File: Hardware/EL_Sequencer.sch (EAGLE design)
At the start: 109 parts, among them U1 LM317, U10 Z0103MN, U11 Z0103MN, U12 Z0103MN, U13 MOC3063S, U14 MOC3063S, U15 MOC3063S, U16 MOC3063S, U17 Z0103MN, U18 Z0103MN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

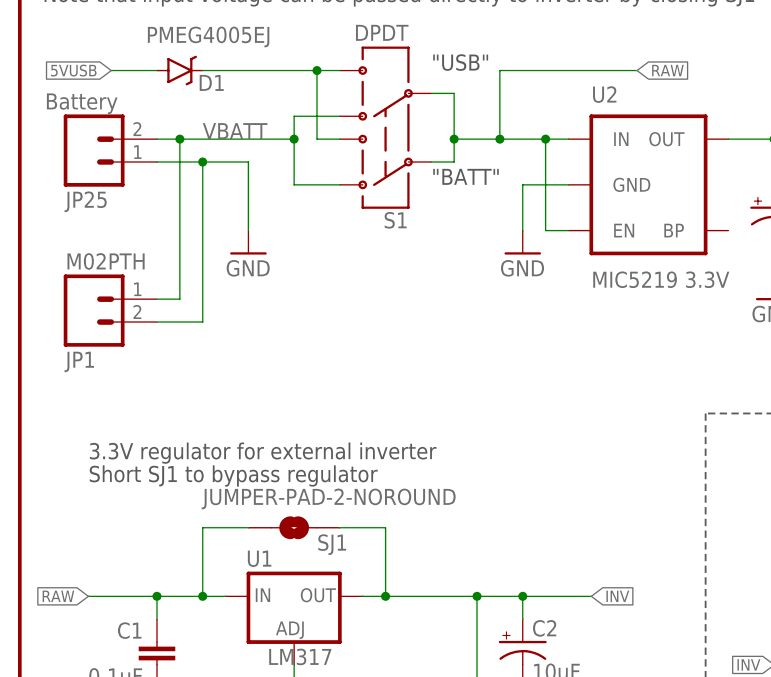
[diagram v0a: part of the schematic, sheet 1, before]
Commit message: Bumping up drill hits in side smd switch
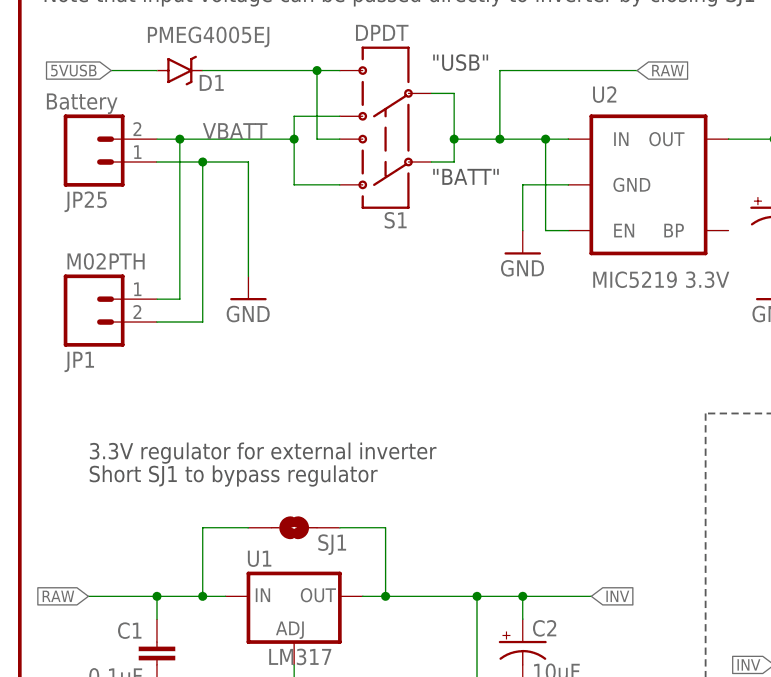
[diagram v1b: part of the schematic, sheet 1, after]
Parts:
- S3: device SparkFun-Electromechanical:SWITCH_SPDT -> Testing:SWITCH_SPDT
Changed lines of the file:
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@@
 <layer number="251" name="SMDround" color="12" fill="11" visible="no" active="no"/>
 <layer number="254" name="cooling" color="7" fill="1" visible="yes" active="yes"/>
+<layer number="255" name="routoute" color="7" fill="1" visible="yes" active="yes"/>
 </layers>
 <schematic xreflabel="%F%N" xrefpart="/%S">
@@
 <part name="FID2" library="SparkFun-Aesthetics" deviceset="FIDUCIAL" device="1X2"/>
 <part name="D1" library="SparkFun-DiscreteSemi" deviceset="DIODE-SCHOTTKY" device="-PMEG4005EJ" value="PMEG4005EJ"/>
-<part name="S3" library="SparkFun-Electromechanical" deviceset="SWITCH_SPDT" device=""/>
+<part name="S3" library="Testing" deviceset="SWITCH_SPDT" device=""/>
 </parts>
 <sheets>
@@
 <attribute name="VALUE" x="2.794" y="162.56" size="1.778" layer="96" rot="MR180"/>
 </instance>
-<instance part="GND1" gate="1" x="25.4" y="144.78"/>
+<instance part="GND1" gate="1" x="25.4" y="139.7"/>
 <instance part="U2" gate="G$1" x="71.12" y="152.4"/>
 <instance part="GND3" gate="1" x="55.88" y="144.78"/>
@@
 <instance part="SJ1" gate="G$1" x="30.48" y="114.3" smashed="yes">
 <attribute name="NAME" x="33.02" y="111.76" size="1.778" layer="95"/>
-<attribute name="VALUE" x="20.32" y="116.84" size="1.778" layer="96"/>
 </instance>
 <instance part="S1" gate="G$1" x="40.64" y="157.48" rot="R180"/>
@@
 <segment>
 <wire x1="20.32" y1="154.94" x2="25.4" y2="154.94" width="0.1524" layer="91"/>
-<wire x1="25.4" y1="154.94" x2="25.4" y2="147.32" width="0.1524" layer="91"/>
+<wire x1="25.4" y1="154.94" x2="25.4" y2="142.24" width="0.1524" layer="91"/>
 <wire x1="20.32" y1="137.16" x2="20.32" y2="154.94" width="0.1524" layer="91"/>
 <pinref part="GND1" gate="1" pin="GND"/>

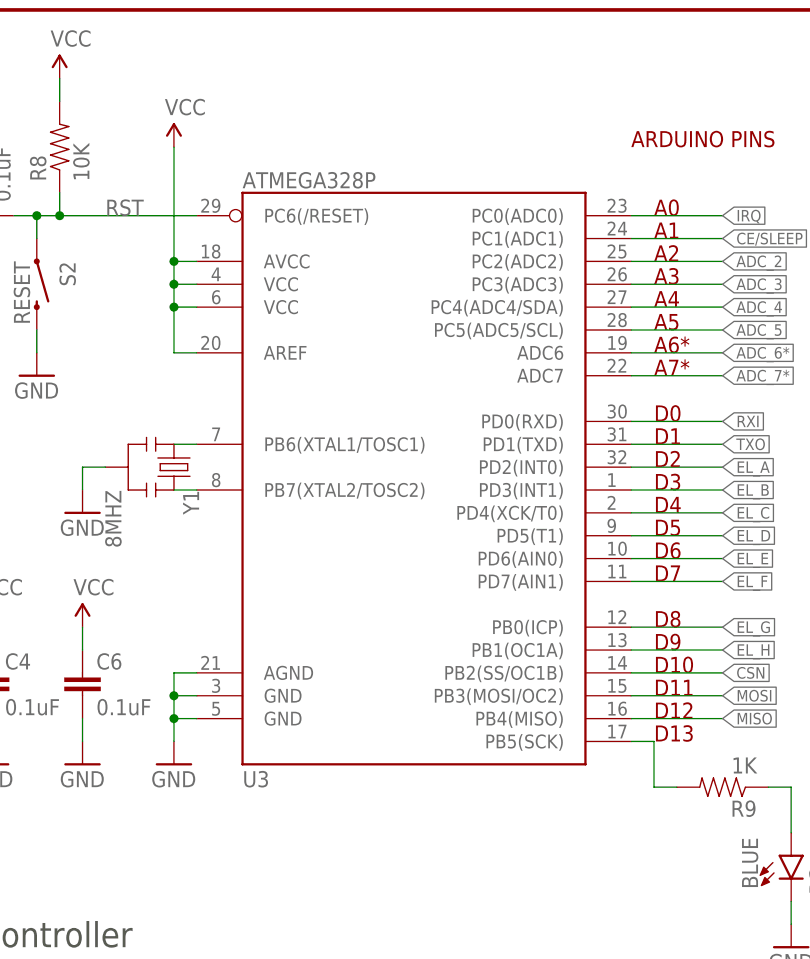
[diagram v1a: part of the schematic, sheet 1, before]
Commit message: Fixing Redboard errors, updating atmega pkg, deleting tvalue name
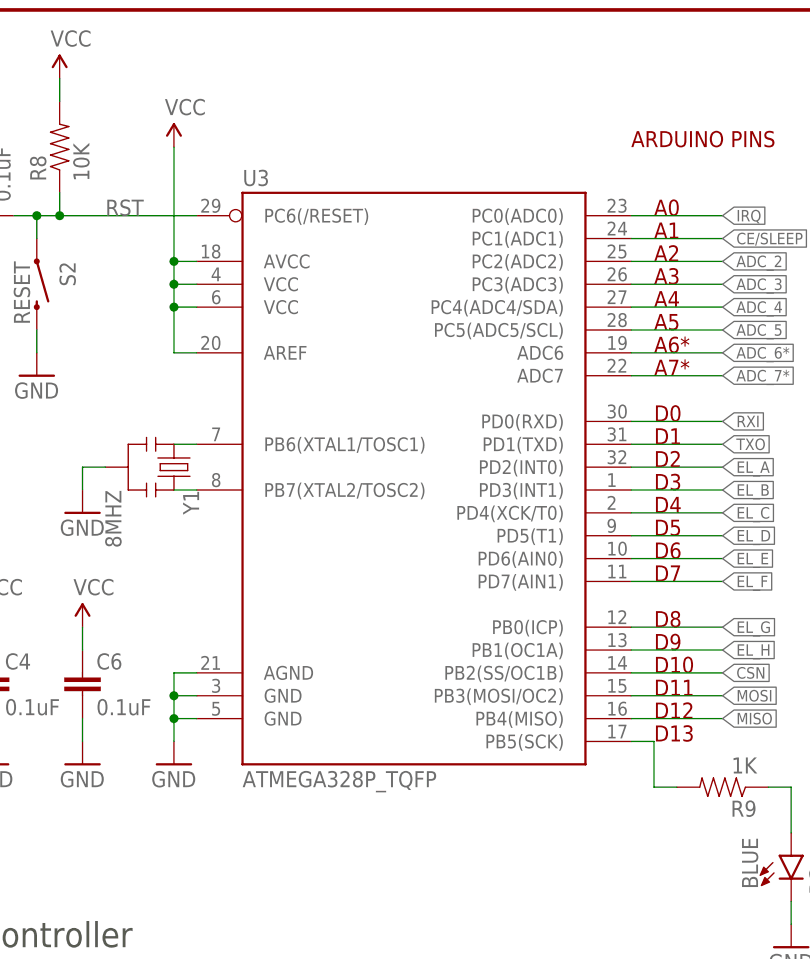
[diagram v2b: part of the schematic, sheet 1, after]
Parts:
- U3: value ATMEGA328P -> ATMEGA328P_TQFP; device SparkFun-DigitalIC:ATMEGA328_SMT -> SparkFun-DigitalIC:ATMEGA328P_TQFP
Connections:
- net GND: now also U3.GND@3, U3.GND@5; no longer U3.GND@1, U3.GND@2
- net VCC: now also U3.VCC@4, U3.VCC@6; no longer U3.VCC@1, U3.VCC@2
